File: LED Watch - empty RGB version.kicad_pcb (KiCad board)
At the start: 2 copper layers, 139 parts, among them J1 AVR-ISP-6, J2 Lipo, J3 Coin Cell, SW1 SW_DPST, SW2 SW_DPST, U1 ATmega165PA-A, U10 B39D3RGB-F6C0001HOU1930, U100 B39D3RGB-F6C0001HOU1930, U101 B39D3RGB-F6C0001HOU1930, U102 B39D3RGB-F6C0001HOU1930, U103 B39D3RGB-F6C0001HOU1930, U104 B39D3RGB-F6C0001HOU1930, U105 B39D3RGB-F6C0001HOU1930, U106 B39D3RGB-F6C0001HOU1930, U107 B39D3RGB-F6C0001HOU1930, U108 B39D3RGB-F6C0001HOU1930, U109 B39D3RGB-F6C0001HOU1930, U11 B39D3RGB-F6C0001HOU1930, U110 B39D3RGB-F6C0001HOU1930, U111 B39D3RGB-F6C0001HOU1930, U112 B39D3RGB-F6C0001HOU1930, U113 B39D3RGB-F6C0001HOU1930, U114 B39D3RGB-F6C0001HOU1930, U115 B39D3RGB-F6C0001HOU1930, U116 B39D3RGB-F6C0001HOU1930, U117 B39D3RGB-F6C0001HOU1930, U118 B39D3RGB-F6C0001HOU1930, U119 B39D3RGB-F6C0001HOU1930, U12 B39D3RGB-F6C0001HOU1930, U120 B39D3RGB-F6C0001HOU1930, U121 B39D3RGB-F6C0001HOU1930, U122 B39D3RGB-F6C0001HOU1930, U123 B39D3RGB-F6C0001HOU1930, U124 B39D3RGB-F6C0001HOU1930, U125 B39D3RGB-F6C0001HOU1930, U126 B39D3RGB-F6C0001HOU1930, U127 B39D3RGB-F6C0001HOU1930, U128 B39D3RGB-F6C0001HOU1930, U129 B39D3RGB-F6C0001HOU1930, U13 B39D3RGB-F6C0001HOU1930, U130 B39D3RGB-F6C0001HOU1930, U131 B39D3RGB-F6C0001HOU1930, U132 B39D3RGB-F6C0001HOU1930, U133 B39D3RGB-F6C0001HOU1930, U134 BMI160, U14 B39D3RGB-F6C0001HOU1930, U15 B39D3RGB-F6C0001HOU1930, U16 B39D3RGB-F6C0001HOU1930, U17 B39D3RGB-F6C0001HOU1930, U18 B39D3RGB-F6C0001HOU1930, U19 B39D3RGB-F6C0001HOU1930, U2 B39D3RGB-F6C0001HOU1930, U20 B39D3RGB-F6C0001HOU1930, U21 B39D3RGB-F6C0001HOU1930, U22 B39D3RGB-F6C0001HOU1930, U23 B39D3RGB-F6C0001HOU1930, U24 B39D3RGB-F6C0001HOU1930, U25 B39D3RGB-F6C0001HOU1930, U26 B39D3RGB-F6C0001HOU1930, U27 B39D3RGB-F6C0001HOU1930, U28 B39D3RGB-F6C0001HOU1930, U29 B39D3RGB-F6C0001HOU1930, U3 B39D3RGB-F6C0001HOU1930, U30 B39D3RGB-F6C0001HOU1930, U31 B39D3RGB-F6C0001HOU1930, U32 B39D3RGB-F6C0001HOU1930, U33 B39D3RGB-F6C0001HOU1930, U34 B39D3RGB-F6C0001HOU1930, U35 B39D3RGB-F6C0001HOU1930, U36 B39D3RGB-F6C0001HOU1930, U37 B39D3RGB-F6C0001HOU1930, U38 B39D3RGB-F6C0001HOU1930, U39 B39D3RGB-F6C0001HOU1930, U4 B39D3RGB-F6C0001HOU1930, U40 B39D3RGB-F6C0001HOU1930, U41 B39D3RGB-F6C0001HOU1930, U42 B39D3RGB-F6C0001HOU1930, U43 B39D3RGB-F6C0001HOU1930, U44 B39D3RGB-F6C0001HOU1930, U45 B39D3RGB-F6C0001HOU1930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

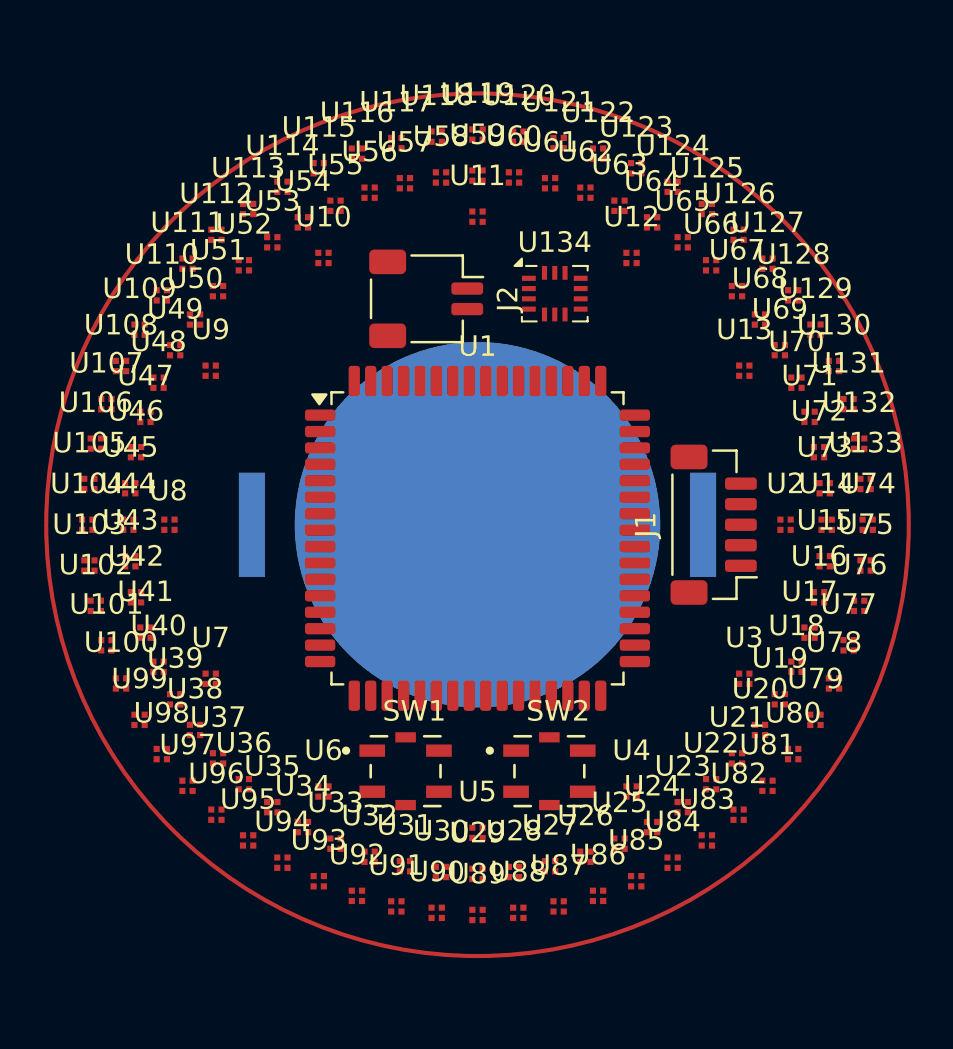
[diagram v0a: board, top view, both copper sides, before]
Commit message: adjusted clocking and spacings.. ready for routing
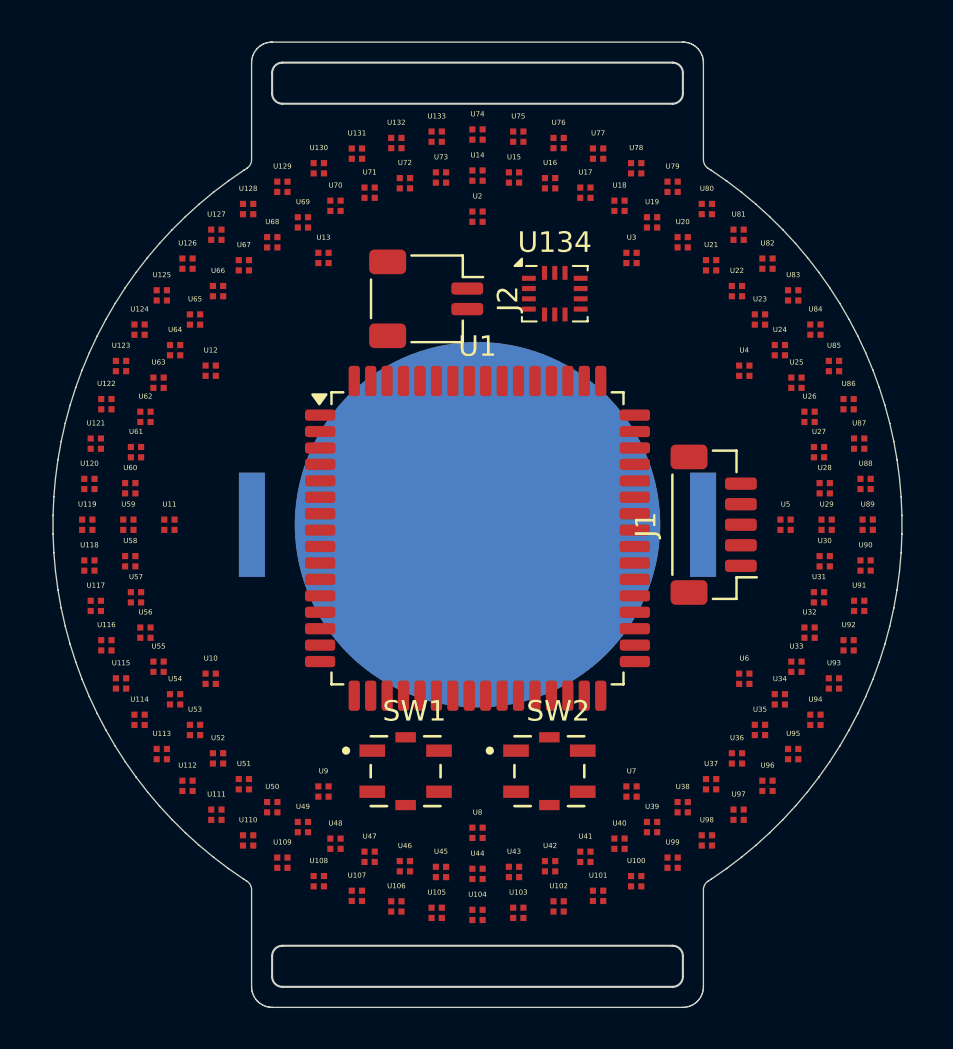
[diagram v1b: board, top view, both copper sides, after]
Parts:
- moved U103 26.9 mm to (102.0, 118.9)
- moved U105 26.9 mm to (98.0, 118.9)
- moved U118 26.9 mm to (81.1, 102.0)
- moved U120 26.9 mm to (81.1, 98.0)
- moved U133 26.9 mm to (98.0, 81.1)
- moved U75 26.9 mm to (102.0, 81.1)
- moved U88 26.9 mm to (118.9, 98.0)
- moved U90 26.9 mm to (118.9, 102.0)
- moved U124 26.9 mm to (83.5, 90.5)
- moved U102 26.9 mm to (104.0, 118.6)
- moved U106 26.9 mm to (96.0, 118.6)
- moved U117 26.9 mm to (81.4, 104.0)
- moved U121 26.9 mm to (81.4, 96.0)
- moved U132 26.9 mm to (96.0, 81.4)
- moved U76 26.9 mm to (104.0, 81.4)
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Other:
- board outline added: 41.3 x 47 mm

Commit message: adjusted clocking and spacings.. ready for routing again
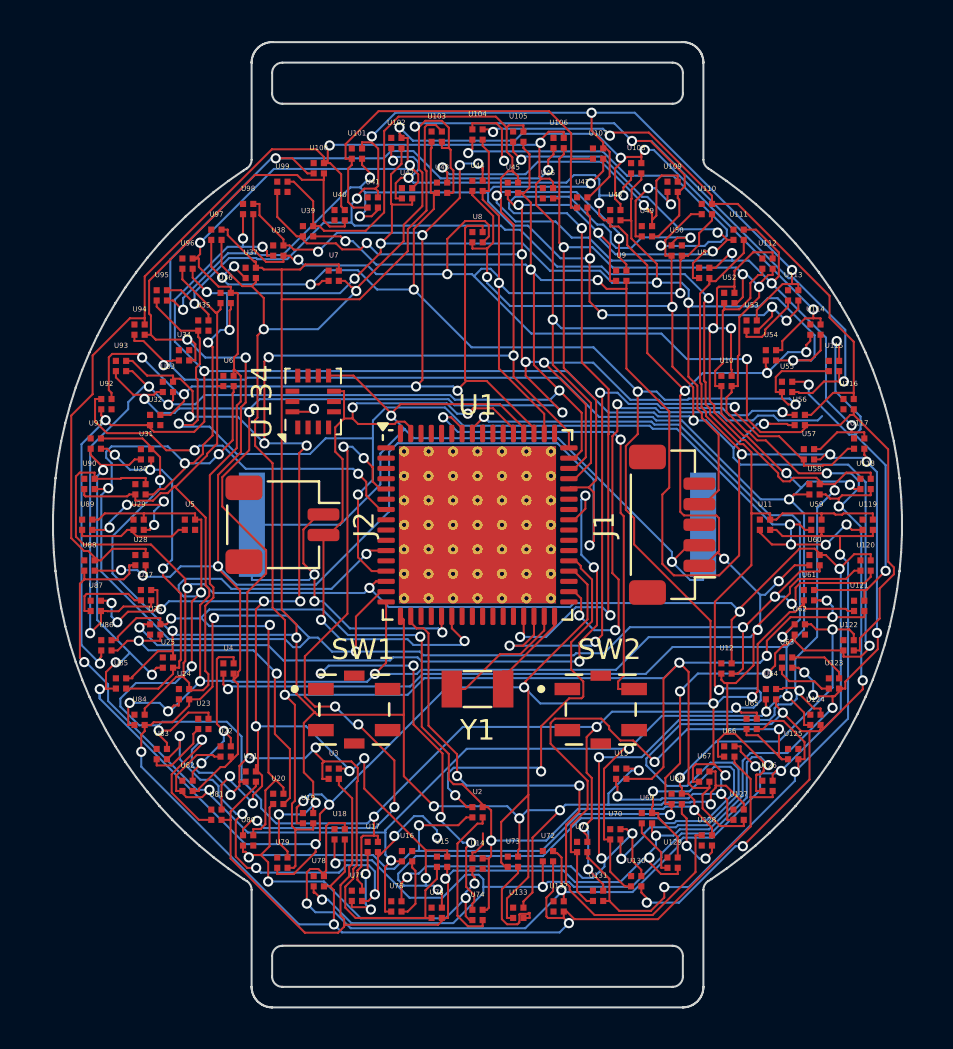
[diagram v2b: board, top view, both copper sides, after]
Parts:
- added Y1: Crystal, Crystal:Crystal_SMD_3215-2Pin_3.2x1.5mm, F.Cu at (100.0, 108.0)
- U1: footprint Package_QFP:TQFP-64_14x14mm_P0.8mm -> Package_DFN_QFN:QFN-64-1EP_9x9mm_P0.5mm_EP7.65x7.65mm_ThermalVias
- moved U126 38.0 mm to (114.1, 112.7)
- moved U127 38.0 mm to (112.7, 114.1)
- moved U112 38.0 mm to (114.1, 87.3)
- moved U81 38.0 mm to (87.3, 114.1)
- moved U111 38.0 mm to (112.7, 85.9)
- moved U82 38.0 mm to (85.9, 112.7)
- moved U96 38.0 mm to (85.9, 87.3)
- moved U97 38.0 mm to (87.3, 85.9)
- moved U123 38.0 mm to (117.4, 107.7)
- moved U130 38.0 mm to (107.7, 117.4)
- moved U115 38.0 mm to (117.4, 92.3)
- moved U78 38.0 mm to (92.3, 117.4)
- moved U108 38.0 mm to (107.7, 82.6)
- moved U85 38.0 mm to (82.6, 107.7)
- moved U100 38.0 mm to (92.3, 82.6)
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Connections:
- U1 pad 31: /Minute9 -> Net-(U1-PD6)
- U1 pad 32: /Minute10 -> Net-(U1-PD7)
- U1 pad 56: unconnected-(U1-PF5-Pad56) -> /Minute10
- U1 pad 57: unconnected-(U1-PF4-Pad57) -> /Minute9
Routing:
- net /G5: track 0.00 -> 210.5 mm, vias 0 -> 19
- net /B3: track 0.00 -> 195.4 mm, vias 0 -> 13
- net /G3: track 0.00 -> 192.0 mm, vias 0 -> 16
- net /R2: track 0.00 -> 190.9 mm, vias 0 -> 23
- net /B1: track 0.00 -> 190.6 mm, vias 0 -> 20
- net /R4: track 0.00 -> 190.3 mm, vias 0 -> 16
- net /G2: track 0.00 -> 189.9 mm, vias 0 -> 17
- net /R5: track 0.00 -> 185.6 mm, vias 0 -> 14
- net /B6: track 0.00 -> 183.1 mm, vias 0 -> 21
- net /B5: track 0.00 -> 182.4 mm, vias 0 -> 18
- net /G6: track 0.00 -> 168.7 mm, vias 0 -> 13
- net /B2: track 0.00 -> 168.6 mm, vias 0 -> 17
- net /R1: track 0.00 -> 167.1 mm, vias 0 -> 17
- net /R6: track 0.00 -> 161.6 mm, vias 0 -> 15
- net /R3: track 0.00 -> 155.2 mm, vias 0 -> 13
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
